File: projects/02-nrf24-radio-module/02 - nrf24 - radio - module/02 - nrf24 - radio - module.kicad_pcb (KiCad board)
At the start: 2 copper layers, 2 parts, among them J1 Conn_01x04_Socket, U1 nRF24L01P

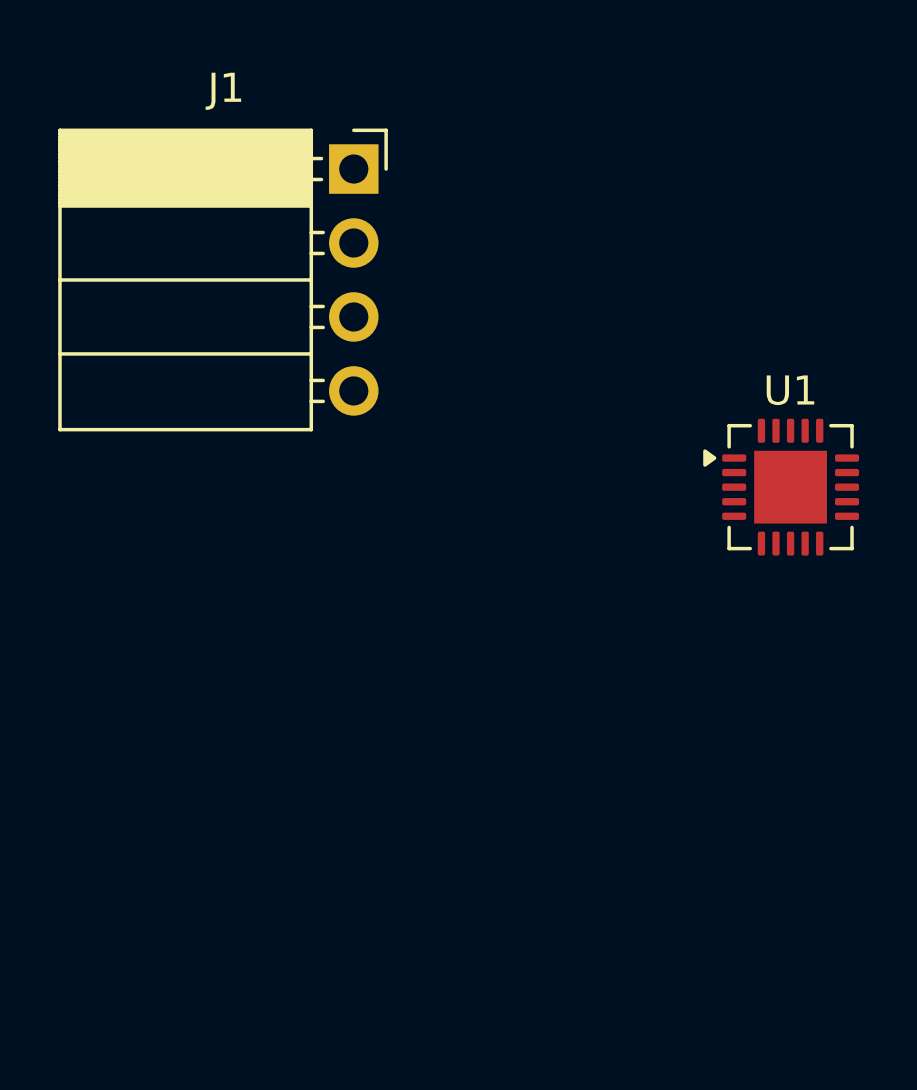
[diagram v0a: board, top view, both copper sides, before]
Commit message: Developing nrf24 board
Simulation of antenna matching and microstrip is started
Added monitor pins for signals to be measured
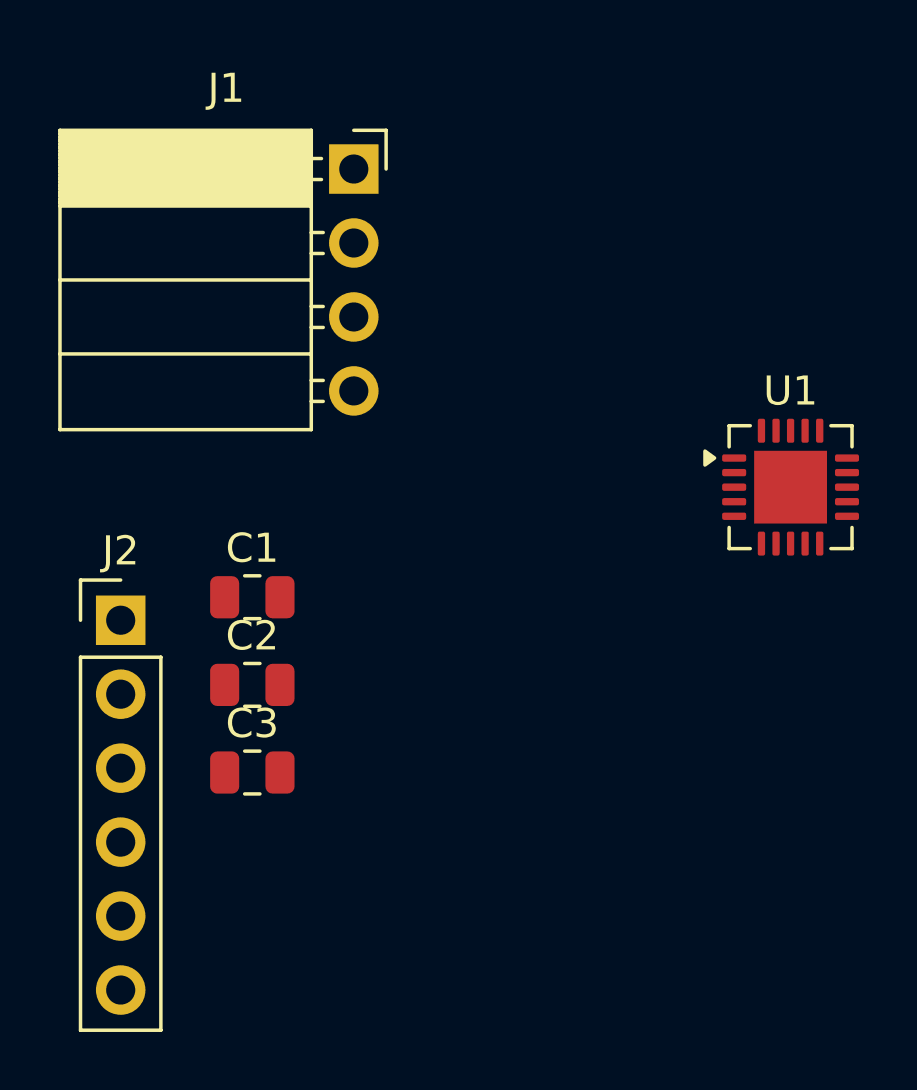
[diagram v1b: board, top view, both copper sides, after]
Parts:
- added C1: 10n, Capacitor_SMD:C_0805_2012Metric, F.Cu at (112.1, 107.2)
- added C2: 1n, Capacitor_SMD:C_0805_2012Metric, F.Cu at (112.1, 110.2)
- added C3: 33n, Capacitor_SMD:C_0805_2012Metric, F.Cu at (112.1, 113.2)
- added J2: MONITOR_Header, Connector_PinHeader_2.54mm:PinHeader_1x06_P2.54mm_Vertical, F.Cu at (107.6, 108.0)
- J1: value Conn_01x04_Socket -> SPI CONNECTOR
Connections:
- U1 pad 1: unconnected-(U1-CE-Pad1) -> CE
- U1 pad 15: unconnected-(U1-VDD-Pad15) -> VDD
- U1 pad 18: unconnected-(U1-VDD-Pad18) -> VDD
- U1 pad 19: unconnected-(U1-DVDD-Pad19) -> Net-(U1-DVDD)
- U1 pad 6: unconnected-(U1-IRQ-Pad6) -> IRQ
- U1 pad 7: unconnected-(U1-VDD-Pad7) -> VDD
